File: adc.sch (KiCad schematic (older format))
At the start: 87 parts, among them U35 MCP6004, U36 MCP6004, U46 MCP6004, U8 MCP6004

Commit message: MRE 0.5.1 panel draft.
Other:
- moved on the sheet: R26, R32, R35, R38, R39, R44, R46, R5, R53, R55, R57, R59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

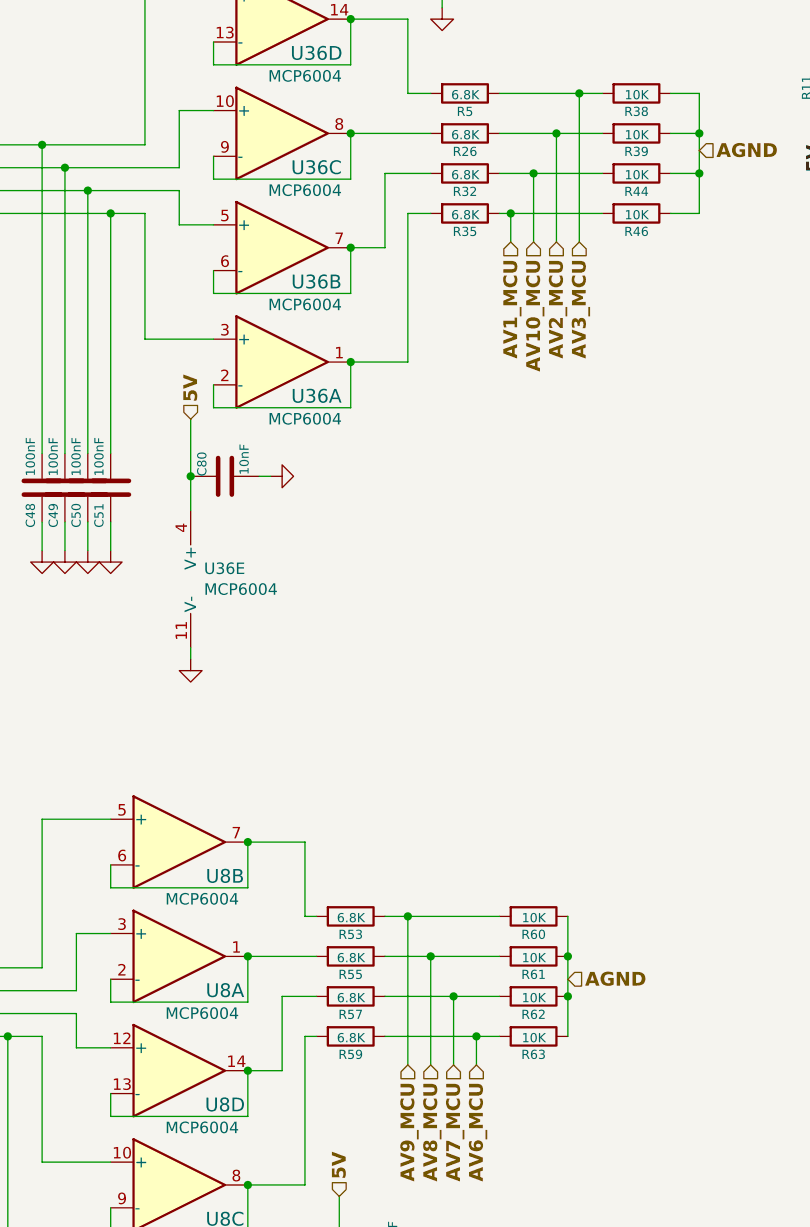
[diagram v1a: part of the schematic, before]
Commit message: AV6, AV8, AV9 and AV10 can now direct drive the digital outputs.
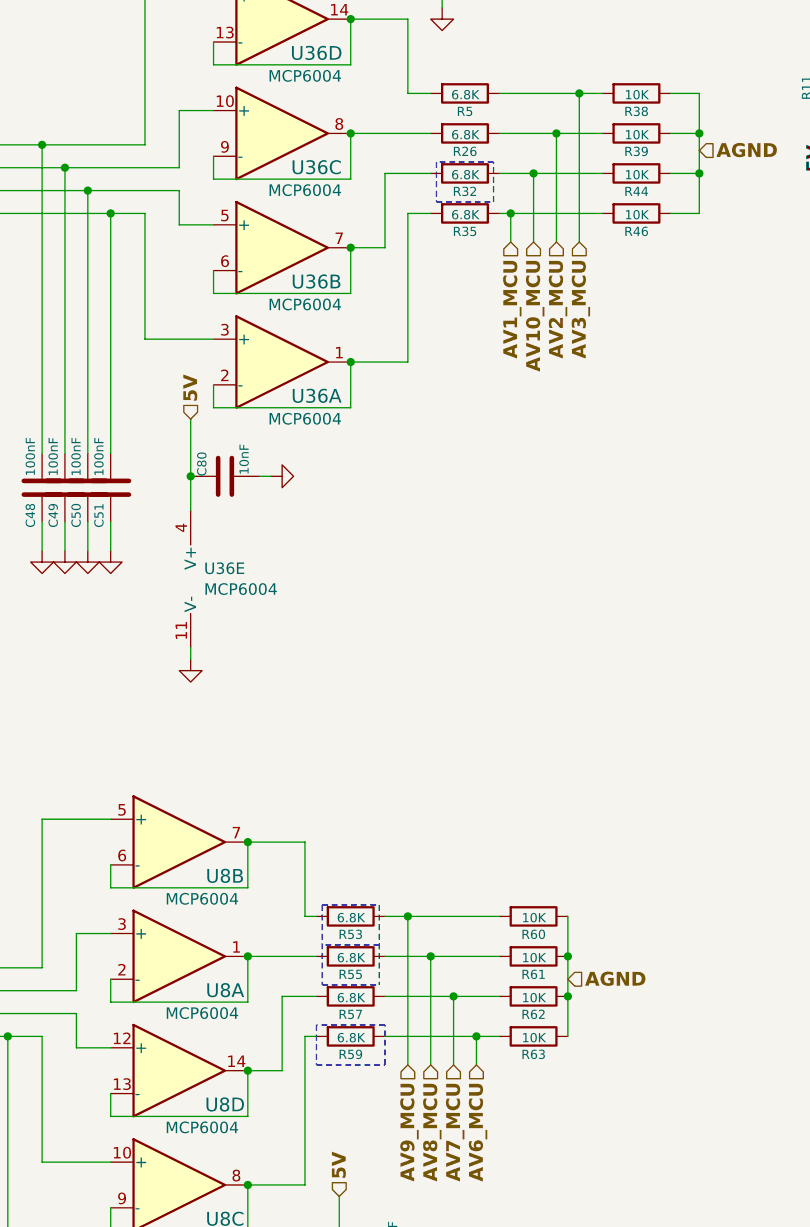
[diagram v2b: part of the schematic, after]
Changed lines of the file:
@@
 Wire Wire Line
 	6950 2050 7225 2050
+Wire Notes Line
+	6800 8600 6800 8775
+Wire Notes Line
+	6800 8775 7100 8775
+Wire Notes Line
+	7100 8775 7100 8600
+Wire Notes Line
+	7100 8600 6800 8600
+Wire Notes Line
+	7325 4825 7325 5000
+Wire Notes Line
+	7325 5000 7575 5000
+Wire Notes Line
+	7575 5000 7575 4825
+Wire Notes Line
+	7575 4825 7325 4825
+Wire Notes Line
+	6825 8425 7075 8425
+Wire Notes Line
+	7075 8250 6825 8250
+Wire Notes Line
+	6825 8075 7075 8075
+Wire Notes Line
+	6825 8075 6825 8425
+Wire Notes Line
+	7075 8075 7075 8425
 $EndSCHEMATC

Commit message: 0.5.1 released
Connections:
- net 12V-SWITCH renamed 12V
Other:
- moved on the sheet: R11, R139, R141, R40
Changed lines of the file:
@@
 P 9250 4500
 F 0 "R131" V 9330 4500 40  0000 C CNN
-F 1 "470K" V 9257 4501 40  0000 C CNN
+F 1 "470K" V 9250 4500 40  0000 C CNN
 F 2 "Resistor_SMD:R_0402_1005Metric" V 11055 3700 60  0001 C CNN
 F 3 "" H 14575 3725 60  0001 C CNN
@@
 L Device:R R139
 U 1 1 5D0E7F1F
-P 10425 4500
-F 0 "R139" V 10505 4500 40  0000 C CNN
-F 1 "39k" V 10432 4501 40  0000 C CNN
-F 2 "Resistor_SMD:R_0603_1608Metric" V 12230 4200 60  0001 C CNN
-F 3 "" H 15750 4225 60  0001 C CNN
-F 4 "RC0603FR-0739KL" H 875 1800 50  0001 C CNN "Part #"
-F 5 "DIGI" H 875 1800 50  0001 C CNN "VEND"
-F 6 "311-39.0KHRCT-ND" H 875 1800 50  0001 C CNN "VEND#"
-F 7 "Yageo" H 875 1800 50  0001 C CNN "Manufacturer"
-F 8 "C23153" H 10425 4500 50  0001 C CNN "LCSC"
-	1    10425 4500
-	-1   0    0    1
+P 10250 4350
+F 0 "R139" V 10330 4350 40  0000 C CNN
+F 1 "39k" V 10250 4350 40  0000 C CNN
+F 2 "Resistor_SMD:R_0603_1608Metric" V 12055 4050 60  0001 C CNN
+F 3 "" H 15575 4075 60  0001 C CNN
+F 4 "RC0603FR-0739KL" H 700 1650 50  0001 C CNN "Part #"
+F 5 "DIGI" H 700 1650 50  0001 C CNN "VEND"
+F 6 "311-39.0KHRCT-ND" H 700 1650 50  0001 C CNN "VEND#"
+F 7 "Yageo" H 700 1650 50  0001 C CNN "Manufacturer"
+F 8 "C23153" H 10250 4350 50  0001 C CNN "LCSC"
+	1    10250 4350
+	0    -1   -1   0
 $EndComp
 $Comp
 L power:GND #PWR0182
 U 1 1 5D0E7F29
-P 10625 4350
-F 0 "#PWR0182" H 10625 4350 30  0001 C CNN
-F 1 "GND" H 10625 4280 30  0001 C CNN
-F 2 "" H 10625 4350 60  0000 C CNN
-F 3 "" H 10625 4350 60  0000 C CNN
-	1    10625 4350
-	-1   0    0    1
+P 10100 4750
+F 0 "#PWR0182" H 10100 4750 30  0001 C CNN
+F 1 "GND" H 10100 4680 30  0001 C CNN
+F 2 "" H 10100 4750 60  0000 C CNN
+F 3 "" H 10100 4750 60  0000 C CNN
+	1    10100 4750
+	-1   0    0    -1
 $EndComp
 $Comp
 L Device:R R141
 U 1 1 5D0E7F36
-P 10625 4500
-F 0 "R141" V 10705 4500 40  0000 C CNN
-F 1 "10K" V 10632 4501 40  0000 C CNN
-F 2 "Resistor_SMD:R_0603_1608Metric" V 12430 3700 60  0001 C CNN
-F 3 "TBD" H 15950 3725 60  0001 C CNN
-F 4 "RMCF0603JT10K0" H 875 1800 50  0001 C CNN "Part #"
-F 5 "DIGI" H 875 1800 50  0001 C CNN "VEND"
-F 6 "RMCF0603JT10K0CT-ND" H 875 1800 50  0001 C CNN "VEND#"
-F 7 "StackPole" H 875 1800 50  0001 C CNN "Manufacturer"
-F 8 "C25804" H 10625 4500 50  0001 C CNN "LCSC"
-	1    10625 4500
-	-1   0    0    1
-$EndComp
-Text HLabel 10425 4350 1    60   Input ~ 12
-12V-SWITCH
+P 10100 4500
+F 0 "R141" V 10180 4500 40  0000 C CNN
+F 1 "10K" V 10100 4500 40  0000 C CNN
+F 2 "Resistor_SMD:R_0603_1608Metric" V 11905 3700 60  0001 C CNN
+F 3 "TBD" H 15425 3725 60  0001 C CNN
+F 4 "RMCF0603JT10K0" H 350 1800 50  0001 C CNN "Part #"
+F 5 "DIGI" H 350 1800 50  0001 C CNN "VEND"
+F 6 "RMCF0603JT10K0CT-ND" H 350 1800 50  0001 C CNN "VEND#"
+F 7 "StackPole" H 350 1800 50  0001 C CNN "Manufacturer"
+F 8 "C25804" H 10100 4500 50  0001 C CNN "LCSC"
+	1    10100 4500
+	1    0    0    -1
+$EndComp
 Text HLabel 14650 3800 3    60   Input ~ 12
 AV11_MCU
@@
 	-1   0    0    1
 $EndComp
-Text Label 9025 4750 3    60   ~ 12
+Text Label 8850 4350 2    60   ~ 12
 5V
 $Comp
 L Device:R R11
 U 1 1 5E614938
-P 9025 4500
-F 0 "R11" V 9105 4500 40  0000 C CNN
-F 1 "DNP" V 9032 4501 40  0000 C CNN
-F 2 "Resistor_SMD:R_0402_1005Metric" V 10830 4200 60  0001 C CNN
-F 3 "" H 14350 4225 60  0001 C CNN
-F 4 "DNP" H 0   0   50  0001 C CNN "Part #"
-F 5 "DIGI" H 0   0   50  0001 C CNN "VEND"
-F 6 "DNP" H 0   0   50  0001 C CNN "VEND#"
-F 7 "DNP" H 0   0   50  0001 C CNN "Manufacturer"
-	1    9025 4500
-	-1   0    0    -1
+P 9100 4350
+F 0 "R11" V 9180 4350 40  0000 C CNN
+F 1 "DNP" V 9100 4350 40  0000 C CNN
+F 2 "Resistor_SMD:R_0402_1005Metric" V 10905 4050 60  0001 C CNN
+F 3 "" H 14425 4075 60  0001 C CNN
+F 4 "DNP" H 75  -150 50  0001 C CNN "Part #"
+F 5 "DIGI" H 75  -150 50  0001 C CNN "VEND"
+F 6 "DNP" H 75  -150 50  0001 C CNN "VEND#"
+F 7 "DNP" H 75  -150 50  0001 C CNN "Manufacturer"
+	1    9100 4350
+	0    1    -1   0
 $EndComp
 $Comp
@@
 P 9950 4500
 F 0 "R41" V 10030 4500 40  0000 C CNN
-F 1 "470K" V 9957 4501 40  0000 C CNN
+F 1 "470K" V 9950 4500 40  0000 C CNN
 F 2 "Resistor_SMD:R_0402_1005Metric" V 11755 3700 60  0001 C CNN
 F 3 "" H 15275 3725 60  0001 C CNN
@@
 	1    0    0    -1
 $EndComp
-Text Label 9700 4750 3    60   ~ 12
+Text Label 9550 4350 2    60   ~ 12
 5V
 $Comp
 L Device:R R40
 U 1 1 5D2DFC9E
-P 9700 4500
-F 0 "R40" V 9780 4500 40  0000 C CNN
-F 1 "DNP" V 9707 4501 40  0000 C CNN
-F 2 "Resistor_SMD:R_0402_1005Metric" V 11505 4200 60  0001 C CNN
-F 3 "" H 15025 4225 60  0001 C CNN
-F 4 "DNP" H 0   0   50  0001 C CNN "Part #"
-F 5 "DIGI" H 0   0   50  0001 C CNN "VEND"
-F 6 "DNP" H 0   0   50  0001 C CNN "VEND#"
-F 7 "DNP" H 0   0   50  0001 C CNN "Manufacturer"
-	1    9700 4500
-	-1   0    0    -1
+P 9800 4350
+F 0 "R40" V 9880 4350 40  0000 C CNN
+F 1 "DNP" V 9800 4350 40  0000 C CNN
+F 2 "Resistor_SMD:R_0402_1005Metric" V 11605 4050 60  0001 C CNN
+F 3 "" H 15125 4075 60  0001 C CNN
+F 4 "DNP" H 100 -150 50  0001 C CNN "Part #"
+F 5 "DIGI" H 100 -150 50  0001 C CNN "VEND"
+F 6 "DNP" H 100 -150 50  0001 C CNN "VEND#"
+F 7 "DNP" H 100 -150 50  0001 C CNN "Manufacturer"
+	1    9800 4350
+	0    1    -1   0
 $EndComp
 Wire Wire Line
@@
 Connection ~ 12700 3500
 Wire Wire Line
-	12800 3600 11575 3600
+	12800 3600 11500 3600
 Connection ~ 12800 3600
-Wire Wire Line
-	9025 4350 9250 4350
-Wire Wire Line
-	9700 4350 9950 4350
-Wire Wire Line
-	10425 4650 10625 4650
 $Comp
 L Device:C C40
@@
 	0    1    1    0
 $EndComp
-Wire Wire Line
-	10100 4650 10425 4650
 $Comp
 L Device:R R35
@@
 $EndComp
 Wire Wire Line
-	11825 4600 11575 4600
-Connection ~ 11575 3600
+	11825 4600 11500 4600
+Connection ~ 11500 3600
 Wire Wire Line
 	12225 4600 12500 4600
@@
 CAM
 Connection ~ 12600 3400
-Connection ~ 10425 4650
 $Comp
 L Power_Protection:NUP4202 D39
@@
 Wire Wire Line
 	9950 4350 9950 3400
-Connection ~ 9950 4350
 Connection ~ 9950 3400
 Wire Wire Line
@@
 Wire Wire Line
 	9250 4350 9250 3500
-Connection ~ 9250 4350
 Connection ~ 9250 3500
 Wire Wire Line
@@
 Connection ~ 9825 3700
 Wire Wire Line
-	10100 4650 10100 3600
+	10100 4350 10100 3600
 Wire Wire Line
 	10100 3600 10650 3600
@@
 	11050 3500 12500 3500
 Wire Wire Line
-	11050 3600 11575 3600
+	11050 3600 11500 3600
 Text Notes 13025 4775 0    50   ~ 0
 Comparator with histeresis for CAM input?\nUsign this OpAmp.
 Wire Wire Line
-	11575 3600 11575 4600
+	11500 3600 11500 4600
 Wire Wire Line
 	4925 3200 5050 3200
@@
 	11050 3400 12400 3400
 Wire Wire Line
-	11050 3700 11650 3700
-Wire Wire Line
-	11825 4400 11650 4400
-Wire Wire Line
-	11650 3700 11650 4400
-Connection ~ 11650 3700
-Wire Wire Line
-	11650 3700 12900 3700
+	11050 3700 11750 3700
+Wire Wire Line
+	11825 4400 11750 4400
+Wire Wire Line
+	11750 3700 11750 4400
+Connection ~ 11750 3700
+Wire Wire Line
+	11750 3700 12900 3700
 Wire Wire Line
 	4550 8350 5150 8350
@@
 	9950 4650 9950 4750
 Wire Wire Line
-	9700 4650 9700 4750
+	9650 4350 9550 4350
 Wire Wire Line
 	9250 4650 9250 4750
 Wire Wire Line
-	9025 4650 9025 4750
+	8950 4350 8850 4350
 Wire Wire Line
 	9825 2550 9825 2600
@@
 Wire Notes Line
 	7075 8075 7075 8425
+Text HLabel 10450 4350 2    60   Input ~ 12
+12V
+Connection ~ 9950 4350
+Connection ~ 9250 4350
+Connection ~ 10100 4350
+Wire Wire Line
+	10100 4750 10100 4650
+Wire Wire Line
+	10400 4350 10450 4350
 $EndSCHEMATC

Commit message: 0.5.1 released
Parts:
- R53, R55: LCSC C23212 -> (none)
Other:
- note added: "NOT OEM POPULATED\nOEM IS \nAV6 AND AV10 ARE ANALOG\nAV8 AND AV9 ARE DIGITAL OUTPUTS"
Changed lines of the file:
@@
 F 2 "Resistor_SMD:R_0603_1608Metric" V 8755 7500 60  0001 C CNN
 F 3 "" H 12275 7525 60  0001 C CNN
-F 4 "C23212" H 6950 8300 50  0001 C CNN "LCSC"
+F 4 "" H 6950 8300 50  0001 C CNN "LCSC"
 	1    6950 8300
 	0    1    1    0
@@
 F 2 "Resistor_SMD:R_0603_1608Metric" V 8755 7325 60  0001 C CNN
 F 3 "" H 12275 7350 60  0001 C CNN
-F 4 "C23212" H 6950 8125 50  0001 C CNN "LCSC"
+F 4 "" H 6950 8125 50  0001 C CNN "LCSC"
 	1    6950 8125
 	0    1    1    0
@@
 Wire Wire Line
 	10400 4350 10450 4350
+Text Notes 7250 7850 0    50   ~ 0
+NOT OEM POPULATED\nOEM IS \nAV6 AND AV10 ARE ANALOG\nAV8 AND AV9 ARE DIGITAL OUTPUTS
+Wire Notes Line
+	7000 8075 7225 7800
 $EndSCHEMATC

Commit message: Draft 0.5.2 corrected BOM 2.7k from 0603 to 0402
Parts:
- R14, R23, R25, R27: LCSC C13167 -> C25885
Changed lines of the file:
@@
 Title "microRusEFI-2L"
 Date "2020-05-24"
-Rev "R0.5.3"
+Rev "R0.5.2"
 Comp "rusEFI.com"
 Comment1 "Donald Becker"
@@
 F 6 "RMCF0603FT2K70CT-ND" H 0   0   50  0001 C CNN "VEND#"
 F 7 "StackPole" H 0   0   50  0001 C CNN "Manufacturer"
-F 8 "C13167" H 2500 1450 50  0001 C CNN "LCSC"
+F 8 "C25885" H 2500 1450 50  0001 C CNN "LCSC"
 	1    2500 1450
 	-1   0    0    1
@@
 F 6 "RMCF0603FT2K70CT-ND" H 0   0   50  0001 C CNN "VEND#"
 F 7 "StackPole" H 0   0   50  0001 C CNN "Manufacturer"
-F 8 "C13167" H 2675 1450 50  0001 C CNN "LCSC"
+F 8 "C25885" H 2675 1450 50  0001 C CNN "LCSC"
 	1    2675 1450
 	-1   0    0    1
@@
 F 6 "RMCF0603FT2K70CT-ND" H 0   0   50  0001 C CNN "VEND#"
 F 7 "StackPole" H 0   0   50  0001 C CNN "Manufacturer"
-F 8 "C13167" H 2850 1450 50  0001 C CNN "LCSC"
+F 8 "C25885" H 2850 1450 50  0001 C CNN "LCSC"
 	1    2850 1450
 	-1   0    0    1
@@
 F 6 "RMCF0603FT2K70CT-ND" H 0   0   50  0001 C CNN "VEND#"
 F 7 "StackPole" H 0   0   50  0001 C CNN "Manufacturer"
-F 8 "C13167" H 3025 1450 50  0001 C CNN "LCSC"
+F 8 "C25885" H 3025 1450 50  0001 C CNN "LCSC"
 	1    3025 1450
 	-1   0    0    1

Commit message: Updated BOM's per https://github.com/rusefi/hw_microRusEfi/issues/184
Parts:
- R14, R23, R25, R27: Manufacturer StackPole -> (none); Part # RMCF0603FT2K70 -> (none); VEND DIGI -> (none); VEND# RMCF0603FT2K70CT-ND -> (none)
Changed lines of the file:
@@
 F 2 "Resistor_SMD:R_0402_1005Metric" V 4305 1150 60  0001 C CNN
 F 3 "" H 7825 1175 60  0001 C CNN
-F 4 "RMCF0603FT2K70" H 0   0   50  0001 C CNN "Part #"
-F 5 "DIGI" H 0   0   50  0001 C CNN "VEND"
-F 6 "RMCF0603FT2K70CT-ND" H 0   0   50  0001 C CNN "VEND#"
-F 7 "StackPole" H 0   0   50  0001 C CNN "Manufacturer"
+F 4 "" H 0   0   50  0001 C CNN "Part #"
+F 5 "" H 0   0   50  0001 C CNN "VEND"
+F 6 "" H 0   0   50  0001 C CNN "VEND#"
+F 7 "" H 0   0   50  0001 C CNN "Manufacturer"
 F 8 "C25885" H 2500 1450 50  0001 C CNN "LCSC"
 	1    2500 1450
@@
 F 2 "Resistor_SMD:R_0402_1005Metric" V 4480 1150 60  0001 C CNN
 F 3 "" H 8000 1175 60  0001 C CNN
-F 4 "RMCF0603FT2K70" H 0   0   50  0001 C CNN "Part #"
-F 5 "DIGI" H 0   0   50  0001 C CNN "VEND"
-F 6 "RMCF0603FT2K70CT-ND" H 0   0   50  0001 C CNN "VEND#"
-F 7 "StackPole" H 0   0   50  0001 C CNN "Manufacturer"
+F 4 "" H 0   0   50  0001 C CNN "Part #"
+F 5 "" H 0   0   50  0001 C CNN "VEND"
+F 6 "" H 0   0   50  0001 C CNN "VEND#"
+F 7 "" H 0   0   50  0001 C CNN "Manufacturer"
 F 8 "C25885" H 2675 1450 50  0001 C CNN "LCSC"
 	1    2675 1450
@@
 F 2 "Resistor_SMD:R_0402_1005Metric" V 4655 1150 60  0001 C CNN
 F 3 "" H 8175 1175 60  0001 C CNN
-F 4 "RMCF0603FT2K70" H 0   0   50  0001 C CNN "Part #"
-F 5 "DIGI" H 0   0   50  0001 C CNN "VEND"
-F 6 "RMCF0603FT2K70CT-ND" H 0   0   50  0001 C CNN "VEND#"
-F 7 "StackPole" H 0   0   50  0001 C CNN "Manufacturer"
+F 4 "" H 0   0   50  0001 C CNN "Part #"
+F 5 "" H 0   0   50  0001 C CNN "VEND"
+F 6 "" H 0   0   50  0001 C CNN "VEND#"
+F 7 "" H 0   0   50  0001 C CNN "Manufacturer"
 F 8 "C25885" H 2850 1450 50  0001 C CNN "LCSC"
 	1    2850 1450
@@
 F 2 "Resistor_SMD:R_0402_1005Metric" V 4830 1150 60  0001 C CNN
 F 3 "" H 8350 1175 60  0001 C CNN
-F 4 "RMCF0603FT2K70" H 0   0   50  0001 C CNN "Part #"
-F 5 "DIGI" H 0   0   50  0001 C CNN "VEND"
-F 6 "RMCF0603FT2K70CT-ND" H 0   0   50  0001 C CNN "VEND#"
-F 7 "StackPole" H 0   0   50  0001 C CNN "Manufacturer"
+F 4 "" H 0   0   50  0001 C CNN "Part #"
+F 5 "" H 0   0   50  0001 C CNN "VEND"
+F 6 "" H 0   0   50  0001 C CNN "VEND#"
+F 7 "" H 0   0   50  0001 C CNN "Manufacturer"
 F 8 "C25885" H 3025 1450 50  0001 C CNN "LCSC"
 	1    3025 1450

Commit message: To many extended parts, switch 2.7k back to basic part, moved pads around to accommodate per https://github.com/rusefi/hw_microRusEfi/issues/184
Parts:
- R14, R23, R25, R27: footprint Resistor_SMD:R_0402_1005Metric -> Resistor_SMD:R_0603_1608Metric; LCSC C25885 -> C13167; Manufacturer (none) -> StackPole; Part # (none) -> RMCF0603FT2K70; VEND (none) -> DIGI; VEND# (none) -> RMCF0603FT2K70CT-ND
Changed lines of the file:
@@
 F 0 "R14" V 2580 1450 40  0000 C CNN
 F 1 "2.7k" V 2507 1451 40  0000 C CNN
-F 2 "Resistor_SMD:R_0402_1005Metric" V 4305 1150 60  0001 C CNN
+F 2 "Resistor_SMD:R_0603_1608Metric" V 4305 1150 60  0001 C CNN
 F 3 "" H 7825 1175 60  0001 C CNN
-F 4 "" H 0   0   50  0001 C CNN "Part #"
-F 5 "" H 0   0   50  0001 C CNN "VEND"
-F 6 "" H 0   0   50  0001 C CNN "VEND#"
-F 7 "" H 0   0   50  0001 C CNN "Manufacturer"
-F 8 "C25885" H 2500 1450 50  0001 C CNN "LCSC"
+F 4 "RMCF0603FT2K70" H 0   0   50  0001 C CNN "Part #"
+F 5 "DIGI" H 0   0   50  0001 C CNN "VEND"
+F 6 "RMCF0603FT2K70CT-ND" H 0   0   50  0001 C CNN "VEND#"
+F 7 "StackPole" H 0   0   50  0001 C CNN "Manufacturer"
+F 8 "C13167" H 2500 1450 50  0001 C CNN "LCSC"
 	1    2500 1450
 	-1   0    0    1
@@
 F 0 "R23" V 2755 1450 40  0000 C CNN
 F 1 "2.7k" V 2682 1451 40  0000 C CNN
-F 2 "Resistor_SMD:R_0402_1005Metric" V 4480 1150 60  0001 C CNN
+F 2 "Resistor_SMD:R_0603_1608Metric" V 4480 1150 60  0001 C CNN
 F 3 "" H 8000 1175 60  0001 C CNN
-F 4 "" H 0   0   50  0001 C CNN "Part #"
-F 5 "" H 0   0   50  0001 C CNN "VEND"
-F 6 "" H 0   0   50  0001 C CNN "VEND#"
-F 7 "" H 0   0   50  0001 C CNN "Manufacturer"
-F 8 "C25885" H 2675 1450 50  0001 C CNN "LCSC"
+F 4 "RMCF0603FT2K70" H 0   0   50  0001 C CNN "Part #"
+F 5 "DIGI" H 0   0   50  0001 C CNN "VEND"
+F 6 "RMCF0603FT2K70CT-ND" H 0   0   50  0001 C CNN "VEND#"
+F 7 "StackPole" H 0   0   50  0001 C CNN "Manufacturer"
+F 8 "C13167" H 2675 1450 50  0001 C CNN "LCSC"
 	1    2675 1450
 	-1   0    0    1
@@
 F 0 "R25" V 2930 1450 40  0000 C CNN
 F 1 "2.7k" V 2857 1451 40  0000 C CNN
-F 2 "Resistor_SMD:R_0402_1005Metric" V 4655 1150 60  0001 C CNN
+F 2 "Resistor_SMD:R_0603_1608Metric" V 4655 1150 60  0001 C CNN
 F 3 "" H 8175 1175 60  0001 C CNN
-F 4 "" H 0   0   50  0001 C CNN "Part #"
-F 5 "" H 0   0   50  0001 C CNN "VEND"
-F 6 "" H 0   0   50  0001 C CNN "VEND#"
-F 7 "" H 0   0   50  0001 C CNN "Manufacturer"
-F 8 "C25885" H 2850 1450 50  0001 C CNN "LCSC"
+F 4 "RMCF0603FT2K70" H 0   0   50  0001 C CNN "Part #"
+F 5 "DIGI" H 0   0   50  0001 C CNN "VEND"
+F 6 "RMCF0603FT2K70CT-ND" H 0   0   50  0001 C CNN "VEND#"
+F 7 "StackPole" H 0   0   50  0001 C CNN "Manufacturer"
+F 8 "C13167" H 2850 1450 50  0001 C CNN "LCSC"
 	1    2850 1450
 	-1   0    0    1
@@
 F 0 "R27" V 3105 1450 40  0000 C CNN
 F 1 "2.7k" V 3032 1451 40  0000 C CNN
-F 2 "Resistor_SMD:R_0402_1005Metric" V 4830 1150 60  0001 C CNN
+F 2 "Resistor_SMD:R_0603_1608Metric" V 4830 1150 60  0001 C CNN
 F 3 "" H 8350 1175 60  0001 C CNN
-F 4 "" H 0   0   50  0001 C CNN "Part #"
-F 5 "" H 0   0   50  0001 C CNN "VEND"
-F 6 "" H 0   0   50  0001 C CNN "VEND#"
-F 7 "" H 0   0   50  0001 C CNN "Manufacturer"
-F 8 "C25885" H 3025 1450 50  0001 C CNN "LCSC"
+F 4 "RMCF0603FT2K70" H 0   0   50  0001 C CNN "Part #"
+F 5 "DIGI" H 0   0   50  0001 C CNN "VEND"
+F 6 "RMCF0603FT2K70CT-ND" H 0   0   50  0001 C CNN "VEND#"
+F 7 "StackPole" H 0   0   50  0001 C CNN "Manufacturer"
+F 8 "C13167" H 3025 1450 50  0001 C CNN "LCSC"
 	1    3025 1450
 	-1   0    0    1
